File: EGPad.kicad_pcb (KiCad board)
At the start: 2 copper layers, 111.1 x 133.3 mm, 67 parts, among them M2 MountingHole_2mm, SW1 Rotary_Encoder_Switch, SW2 Rotary_Encoder_Switch, SW3 Rotary_Encoder_Switch, U1 ProMicro

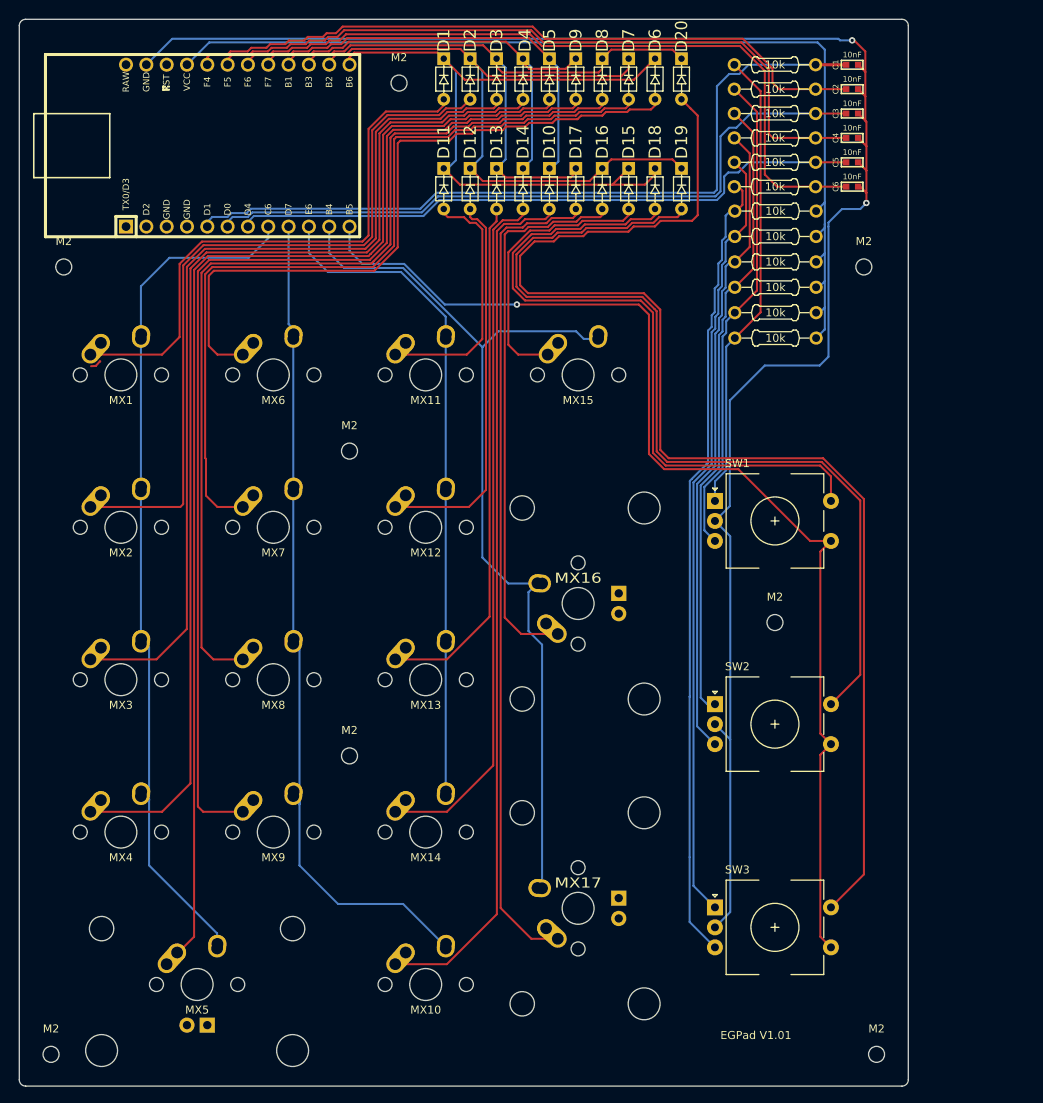
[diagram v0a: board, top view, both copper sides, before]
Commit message: adding oled from Corne style and reverse PCB
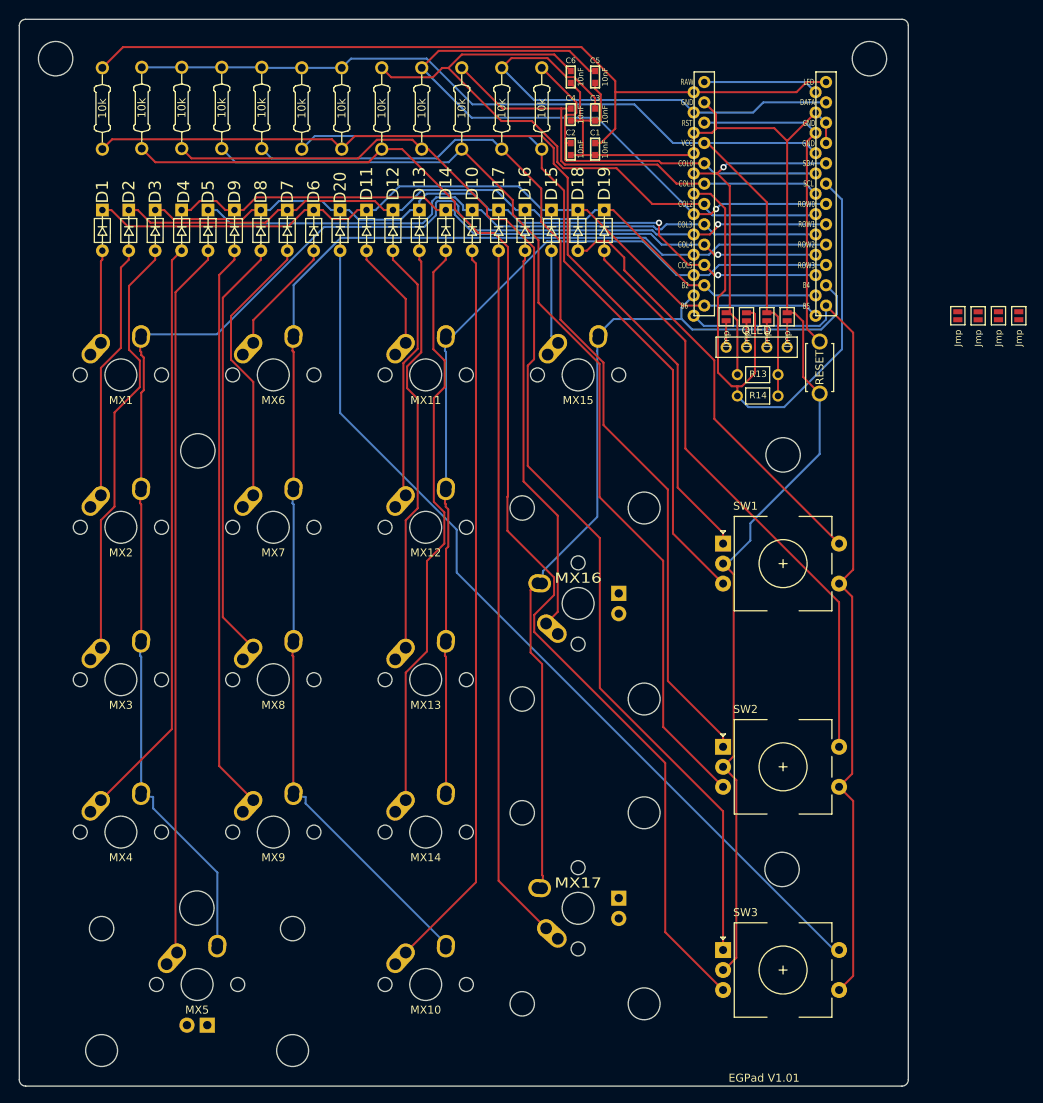
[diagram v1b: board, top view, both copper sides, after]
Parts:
- removed M2 (x8): MountingHole_2mm, MountingHole:MountingHole_2mm
- added J1: OLED, kbd:OLED, F.Cu at (178.1, 70.4)
- added JP1: Jmp, kbd:Jumper, F.Cu at (214.6, 66.4)
- added JP1: Jmp, kbd:Jumper, F.Cu at (185.7, 66.5)
- added JP2: Jmp, kbd:Jumper, F.Cu at (212.1, 66.4)
- added JP2: Jmp, kbd:Jumper, F.Cu at (183.1, 66.5)
- added JP3: Jmp, kbd:Jumper, F.Cu at (209.6, 66.4)
- added JP3: Jmp, kbd:Jumper, F.Cu at (180.6, 66.6)
- added JP4: Jmp, kbd:Jumper, F.Cu at (207.0, 66.4)
- added JP4: Jmp, kbd:Jumper, F.Cu at (178.1, 66.5)
- added R13: R, kbd:R, F.Cu at (182.0, 73.8)
- added R14: R, kbd:R, F.Cu at (182.0, 76.5)
- added RSW1: SW_Push, kbd:ResetSW, F.Cu at (189.7, 72.9)
- added Ref**1: Val**, kbd:M2_HOLE_v2, F.Cu at (196.0, 34.3)
- added Ref**2: Val**, kbd:M2_HOLE_v2, F.Cu at (94.2, 34.3)
- added Ref**3: Val**, kbd:M2_HOLE_v2, F.Cu at (185.2, 83.8)
- added Ref**4: Val**, kbd:M2_HOLE_v2, F.Cu at (112.0, 83.3)
- added Ref**5: Val**, kbd:M2_HOLE_v2, F.Cu at (111.9, 140.5)
- added Ref**6: Val**, kbd:M2_HOLE_v2, F.Cu at (185.0, 135.6)
- U1: footprint Keebio Footprints:ArduinoProMicro-Mini-USB -> kbd:ProMicro_v2
- moved R1 84.3 mm to (100.1, 40.5), turned to 270 degrees
- moved R12 80.3 mm to (105.0, 40.4), turned to 270 degrees
- moved R11 75.9 mm to (110.0, 40.4), turned to 270 degrees
- moved R10 71.8 mm to (115.0, 40.4), turned to 270 degrees
- moved R9 68.0 mm to (120.0, 40.4), turned to 270 degrees
- moved U1 66.2 mm to (182.9, 51.7)
- moved R8 64.5 mm to (125.0, 40.5), turned to 270 degrees
- moved R7 61.3 mm to (130.0, 40.5), turned to 270 degrees
- moved R6 50.1 mm to (135.0, 40.5), turned to 270 degrees
- moved D2 46.7 mm to (103.4, 51.9)
- moved D9 46.7 mm to (116.6, 51.9)
- moved D1 46.7 mm to (100.1, 51.9)
- moved D20 46.7 mm to (129.8, 51.9)
- moved D3 46.7 mm to (106.7, 51.9)
- moved D4 46.7 mm to (110.0, 51.9)
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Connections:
- U1 pad 1: Net-(U1-Pad1) -> A1
- U1 pad 2: Net-(U1-Pad2) -> A2
- U1 pad 22: Net-(U1-Pad22) -> reset
- U1 pad 3: Net-(U1-Pad3) -> GND
- U1 pad 4: Net-(U1-Pad4) -> GND
- U1 pad 5: A1 -> SDA
- U1 pad 6: A2 -> SCL
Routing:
- net SCL: track 0.00 -> 79.5 mm
- net Net-(D6-Pad2): track 86.5 -> 16.7 mm
- net COL1: track 109.9 -> 178.4 mm, vias 0 -> 1
- net Net-(D7-Pad2): track 103.2 -> 36.6 mm
- net Net-(D8-Pad2): track 119.9 -> 55.2 mm
- net Net-(D9-Pad2): track 137.2 -> 73.2 mm
- net Net-(D4-Pad2): track 136.8 -> 74.9 mm
- net Net-(D2-Pad2): track 93.9 -> 34.0 mm
- net Net-(D3-Pad2): track 114.5 -> 55.6 mm
- net Net-(R1-Pad2): track 58.7 -> 116.9 mm
- net Net-(D5-Pad2): track 149.7 -> 91.5 mm
- net Net-(R12-Pad2): track 101.5 -> 158.9 mm
- net Net-(D1-Pad2): track 71.0 -> 13.6 mm
- net COL2: track 105.1 -> 162.3 mm
- net Net-(R11-Pad2): track 97.8 -> 149.9 mm
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
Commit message: optimization and gerber for production
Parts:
- removed the JP1 at (214.6, 66.4)
- removed the JP2 at (212.1, 66.4)
- removed the JP3 at (209.6, 66.4)
- removed the JP4 at (207.0, 66.4)
- removed Ref**3: Val**, kbd:M2_HOLE_v2
- added JP5: Jmp, kbd:Jumper, B.Cu at (185.7, 66.5)
- added JP6: Jmp, kbd:Jumper, B.Cu at (183.1, 66.6)
- added JP7: Jmp, kbd:Jumper, B.Cu at (180.6, 66.5)
- added JP8: Jmp, kbd:Jumper, B.Cu at (178.1, 66.5)
- added Ref**: Val**, kbd:M2_HOLE_v2, F.Cu at (111.9, 83.4)
- moved Ref**4 73.0 mm to (185.0, 84.6)
- moved Ref**1 1.09 mm to (195.3, 35.2)
- moved Ref**2 0.99 mm to (95.0, 34.9)
- moved Ref**5 0.18 mm to (112.0, 140.6)
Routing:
- net COL3: track 112.8 -> 150.0 mm
- net SDA: track 43.7 -> 78.5 mm, vias 1 -> 0
- net GND: track 175.9 -> 200.0 mm
- net SCL: track 79.5 -> 97.5 mm
- net VCC: track 125.8 -> 137.8 mm
- net B2: track 55.8 -> 66.5 mm
- net A3: track 82.2 -> 71.7 mm, vias 1 -> 0
- net A2: track 58.9 -> 51.2 mm
- net B3: track 81.1 -> 87.7 mm, vias 0 -> 1
- net B1: track 47.2 -> 52.7 mm
- net COL1: track 178.4 -> 174.0 mm
- net Net-(J1-Pad4): track 3.31 -> 6.62 mm
- net Net-(J1-Pad2): track 3.30 -> 6.61 mm
- net Net-(J1-Pad1): track 3.31 -> 6.62 mm
- net Net-(J1-Pad3): track 3.31 -> 6.61 mm
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- added copper zone on B.Cu, net GND
- added copper zone on F.Cu, net GND
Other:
- board text added: "EGPad Oled V1.0"
- board text removed: "EGPad V1.01"
